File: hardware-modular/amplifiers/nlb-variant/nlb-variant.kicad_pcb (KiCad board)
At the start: 2 copper layers, 60 x 40 mm, 21 parts, among them J1 DC_IN, J2 RF_IN, J3 RF_OUT, U1 NLB-310

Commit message: Tweaked amplifier modules.
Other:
- board text added: "IN"
- board text added: "OUT"

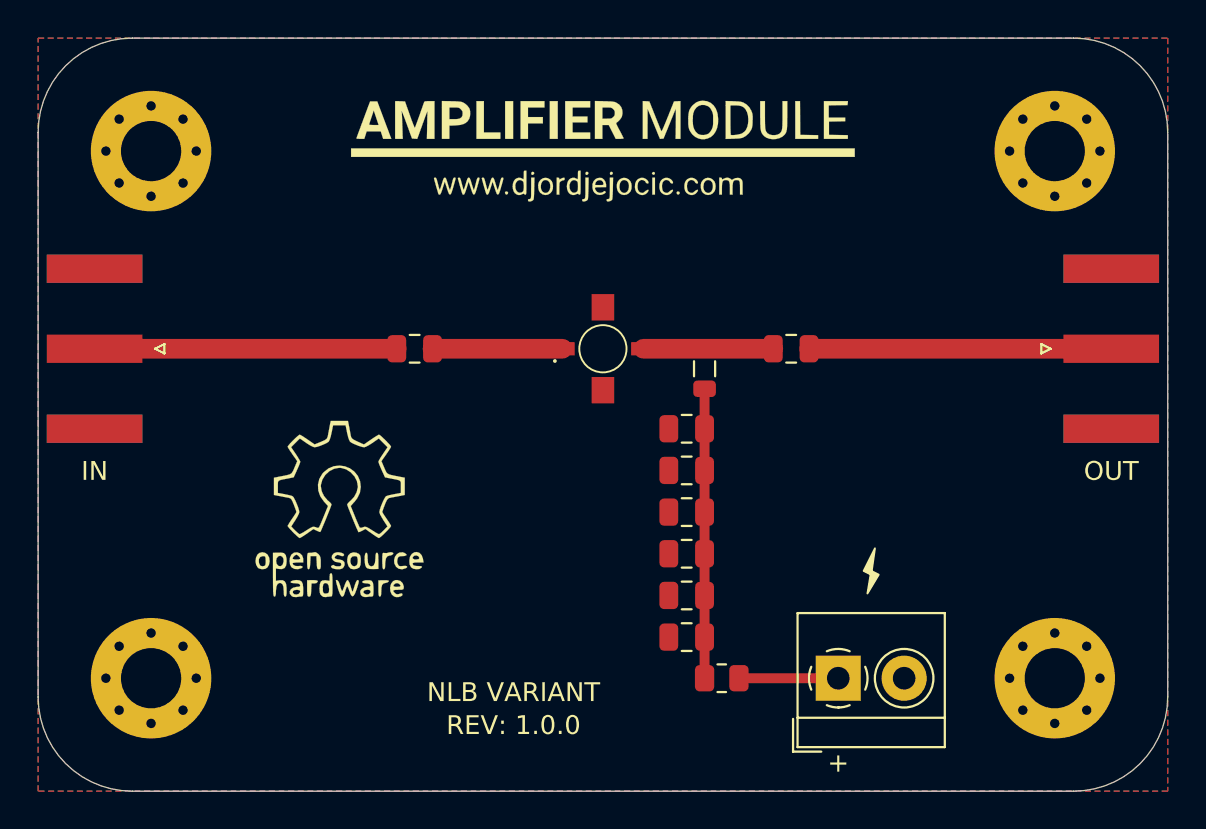
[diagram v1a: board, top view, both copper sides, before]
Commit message: Trans. line width issue resolved - amp. modules.
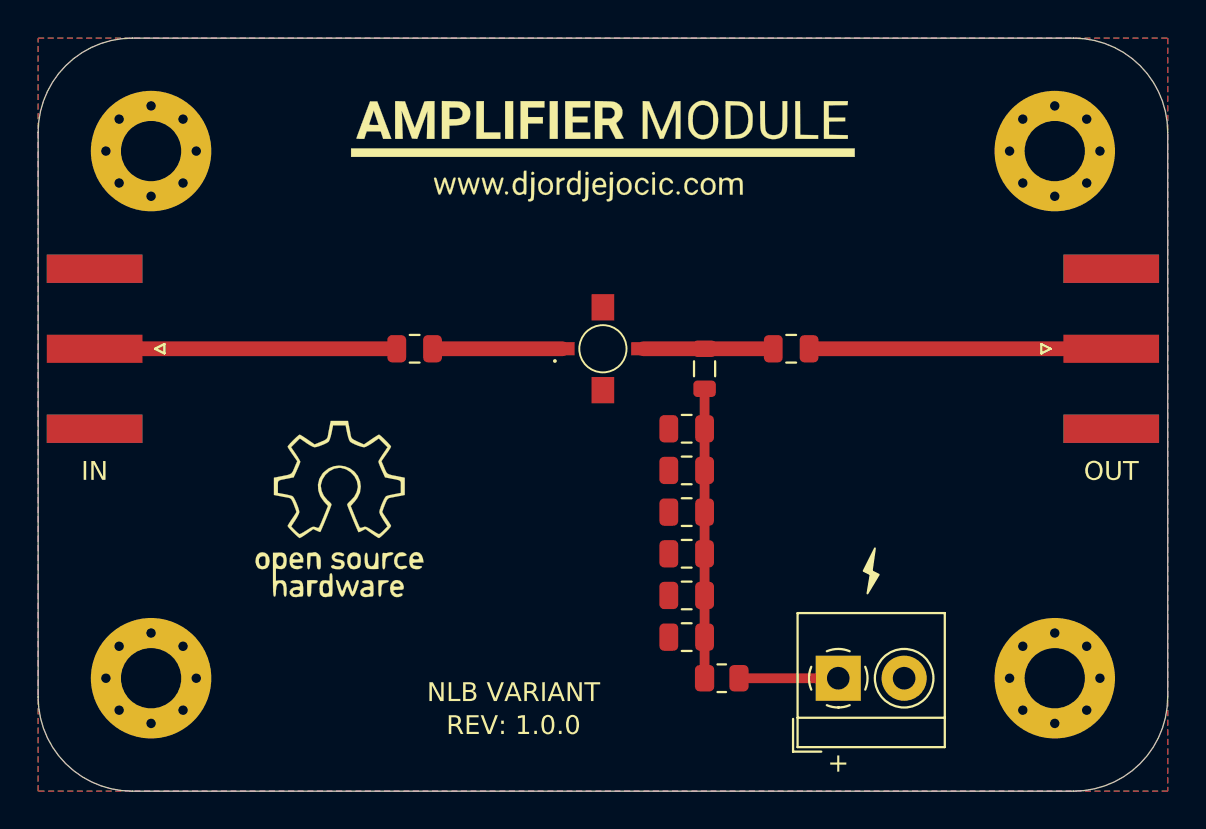
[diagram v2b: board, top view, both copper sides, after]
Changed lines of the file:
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@@
   (general
     (thickness 1.6)
-    (drawings 19)
-    (tracks 6)
+    (drawings 20)
+    (tracks 7)
     (zones 0)
     (modules 21)
@@
   )
   (setup
-    (last_trace_width 0.525491)
+    (last_trace_width 0.784566)
     (user_trace_width 0.525491)
-    (user_trace_width 1.04516)
+    (user_trace_width 0.784566)
     (trace_clearance 0.2)
-    (zone_clearance 0.2)
+    (zone_clearance 0.15)
     (zone_45_only no)
     (trace_min 0.2)
@@
     )
   )
+  (gr_line (start 135.4 66.5) (end 139.05 66.5) (layer F.Mask) (width 1.084566))
+  (gr_line (start 132.15 66.5) (end 135.4 66.5) (layer F.Mask) (width 1.084566))
+  (gr_line (start 140.95 66.5) (end 157 66.5) (layer F.Mask) (width 1.084566))
+  (gr_line (start 120.95 66.5) (end 127.85 66.5) (layer F.Mask) (width 1.084566))
+  (gr_line (start 119.05 66.5) (end 103 66.5) (layer F.Mask) (width 1.084566))
   (gr_text OUT (at 157 73) (layer F.SilkS)
     (effects (font (size 1 1) (thickness 0.12)))
@@
     (effects (font (size 1 1) (thickness 0.12)))
   )
-  (gr_line (start 132.15 66.5) (end 139.05 66.5) (layer F.Mask) (width 1.44516))
-  (gr_line (start 120.95 66.5) (end 127.85 66.5) (layer F.Mask) (width 1.44516))
   (gr_text "REV: 1.0.0" (at 125.25 86.5) (layer F.SilkS)
     (effects (font (size 1 1) (thickness 0.12)))
@@
     (effects (font (size 1 1) (thickness 0.12)))
   )
-  (gr_line (start 140.95 66.5) (end 157 66.5) (layer F.Mask) (width 1.44516))
-  (gr_line (start 119.05 66.5) (end 103 66.5) (layer F.Mask) (width 1.44516))
   (dimension 60 (width 0.15) (layer Dwgs.User)
     (gr_text "60.000 mm" (at 130 43.7) (layer Dwgs.User)
@@
   (gr_line (start 105 50) (end 155 50) (layer Edge.Cuts) (width 0.05))
   (segment (start 142.5 84) (end 137.225 84) (width 0.525491) (layer F.Cu) (net 1))
-  (segment (start 119.05 66.5) (end 103 66.5) (width 1.04516) (layer F.Cu) (net 3))
-  (segment (start 120.95 66.5) (end 127.85 66.5) (width 1.04516) (layer F.Cu) (net 4))
-  (segment (start 140.95 66.5) (end 157 66.5) (width 1.04516) (layer F.Cu) (net 5))
-  (segment (start 132.15 66.5) (end 139.05 66.5) (width 1.04516) (layer F.Cu) (net 6))
+  (segment (start 119.05 66.5) (end 103 66.5) (width 0.784566) (layer F.Cu) (net 3))
+  (segment (start 120.95 66.5) (end 127.85 66.5) (width 0.784566) (layer F.Cu) (net 4))
+  (segment (start 140.95 66.5) (end 157 66.5) (width 0.784566) (layer F.Cu) (net 5))
+  (segment (start 132.15 66.5) (end 135.4 66.5) (width 0.784566) (layer F.Cu) (net 6))
+  (segment (start 135.4 66.5) (end 139.05 66.5) (width 0.784566) (layer F.Cu) (net 6))
   (segment (start 135.4 68.625) (end 135.4 84) (width 0.525491) (layer F.Cu) (net 7))
   (zone (net 2) (net_name GND) (layer F.Cu) (hatch edge 0.508)
-    (connect_pads yes (clearance 0.2))
-    (min_thickness 0.1)
-    (fill yes (arc_segments 32) (thermal_gap 0.2) (thermal_bridge_width 0.2))
+    (connect_pads yes (clearance 0.15))
+    (min_thickness 0.075)
+    (fill yes (arc_segments 32) (thermal_gap 0.15) (thermal_bridge_width 0.15))
     (polygon
       (pts
@@
   )
   (zone (net 2) (net_name GND) (layer B.Cu) (hatch edge 0.508)
-    (connect_pads yes (clearance 0.2))
-    (min_thickness 0.1)
-    (fill yes (arc_segments 32) (thermal_gap 0.2) (thermal_bridge_width 0.2))
+    (connect_pads yes (clearance 0.15))
+    (min_thickness 0.075)
+    (fill yes (arc_segments 32) (thermal_gap 0.15) (thermal_bridge_width 0.15))
     (polygon
       (pts
